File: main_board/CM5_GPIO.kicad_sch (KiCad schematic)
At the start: 32 parts, among them IC4 TS921ID, IC6 TS921ID, J8 AudioJack3

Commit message: Add mounting points to symbols
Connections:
- net GND: now also Module1.MP
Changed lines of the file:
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@@
+	)
+	(junction
+		(at 93.98 160.02)
+		(diameter 0)
+		(color 0 0 0 0)
 	)
 	(junction
@@
 	)
 	(junction
+		(at 59.69 160.02)
+		(diameter 0)
+		(color 0 0 0 0)
+	)
+	(junction
 		(at 59.69 93.98)
 		(diameter 1.016)
@@
 	)
 	(junction
+		(at 123.19 160.02)
+		(diameter 0)
+		(color 0 0 0 0)
+	)
+	(junction
 		(at 123.19 119.38)
 		(diameter 1.016)
@@
 	(wire
 		(pts
+			(xy 59.69 160.02) (xy 93.98 160.02)
+		)
+		(stroke
+			(width 0)
+			(type default)
+		)
+	)
+	(wire
+		(pts
 			(xy 121.92 154.94) (xy 181.61 154.94)
 		)
@@
 			(width 0)
 			(type solid)
+		)
+	)
+	(wire
+		(pts
+			(xy 93.98 160.02) (xy 123.19 160.02)
+		)
+		(stroke
+			(width 0)
+			(type default)
 		)
 	)
@@
 		(pin "200"
 		)
+		(pin "MP"
+		)
 		(instances

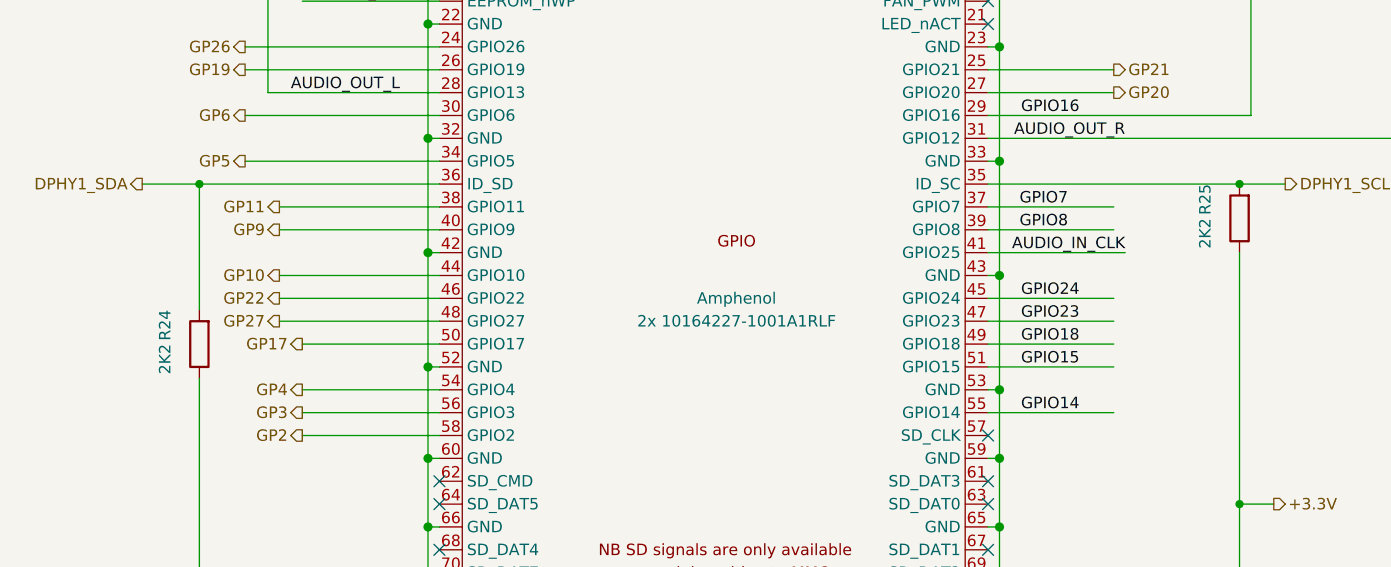
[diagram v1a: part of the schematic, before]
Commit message: Fix bad output voltage
For some reason I got 5V with previous values on prototype. Weird...
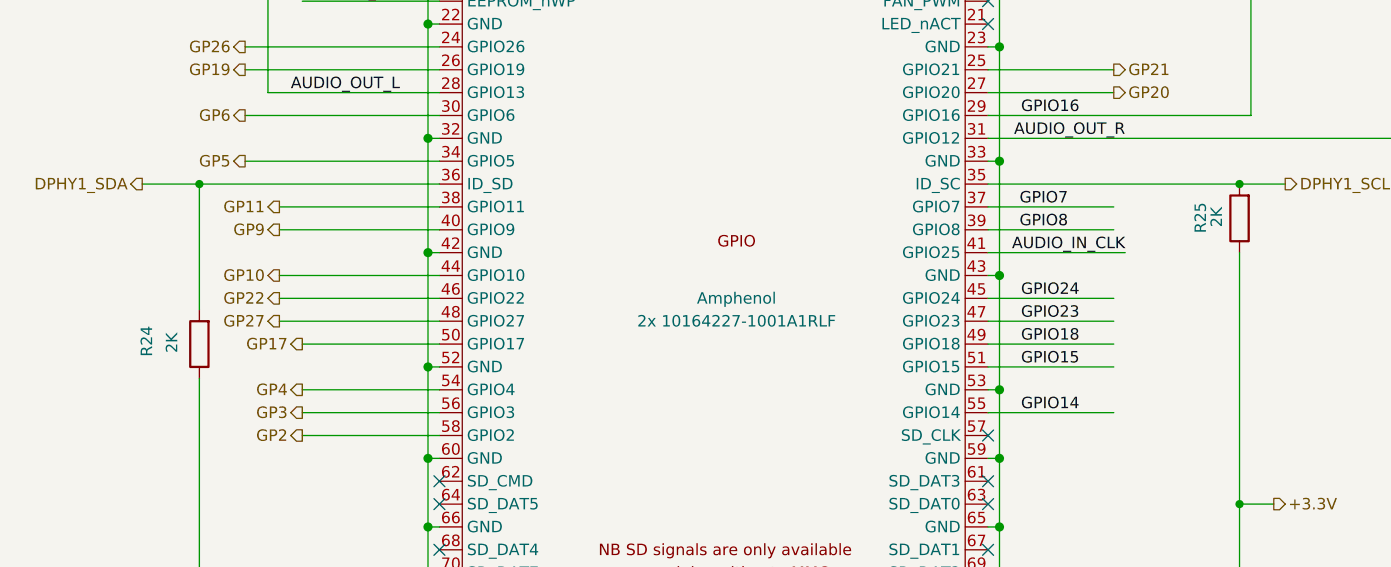
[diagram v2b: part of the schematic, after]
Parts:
- R24, R25: value 2K2 -> 2K
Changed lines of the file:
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@@
 		(dnp no)
 		(property "Reference" "R24"
-			(at 30.48 87.63 90)
+			(at 28.448 89.408 90)
 			(effects
 				(font
@@
 			)
 		)
-		(property "Value" "2K2"
-			(at 30.48 91.44 90)
+		(property "Value" "2K"
+			(at 31.242 90.17 90)
 			(effects
 				(font
@@
 		(dnp no)
 		(property "Reference" "R25"
-			(at 146.05 73.66 90)
+			(at 145.542 75.692 90)
 			(effects
 				(font
@@
 			)
 		)
-		(property "Value" "2K2"
-			(at 146.05 77.47 90)
+		(property "Value" "2K"
+			(at 147.32 76.2 90)
 			(effects
 				(font

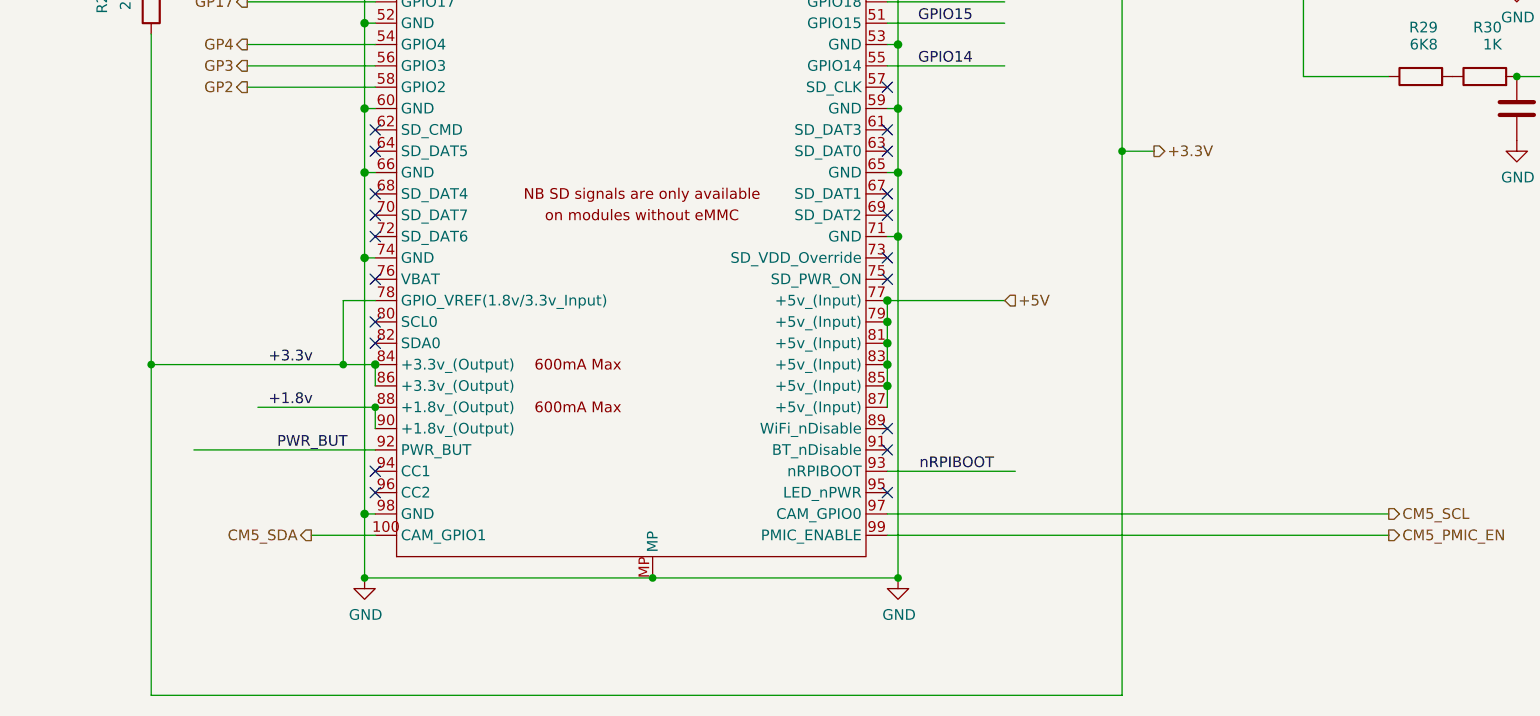
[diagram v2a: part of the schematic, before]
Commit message: Fix critical problems
- Adding USB2 hub on USB3 port did not work correctly
- PM I2C bus was not working when CM5 is shut down
- Missing OTG ID pin
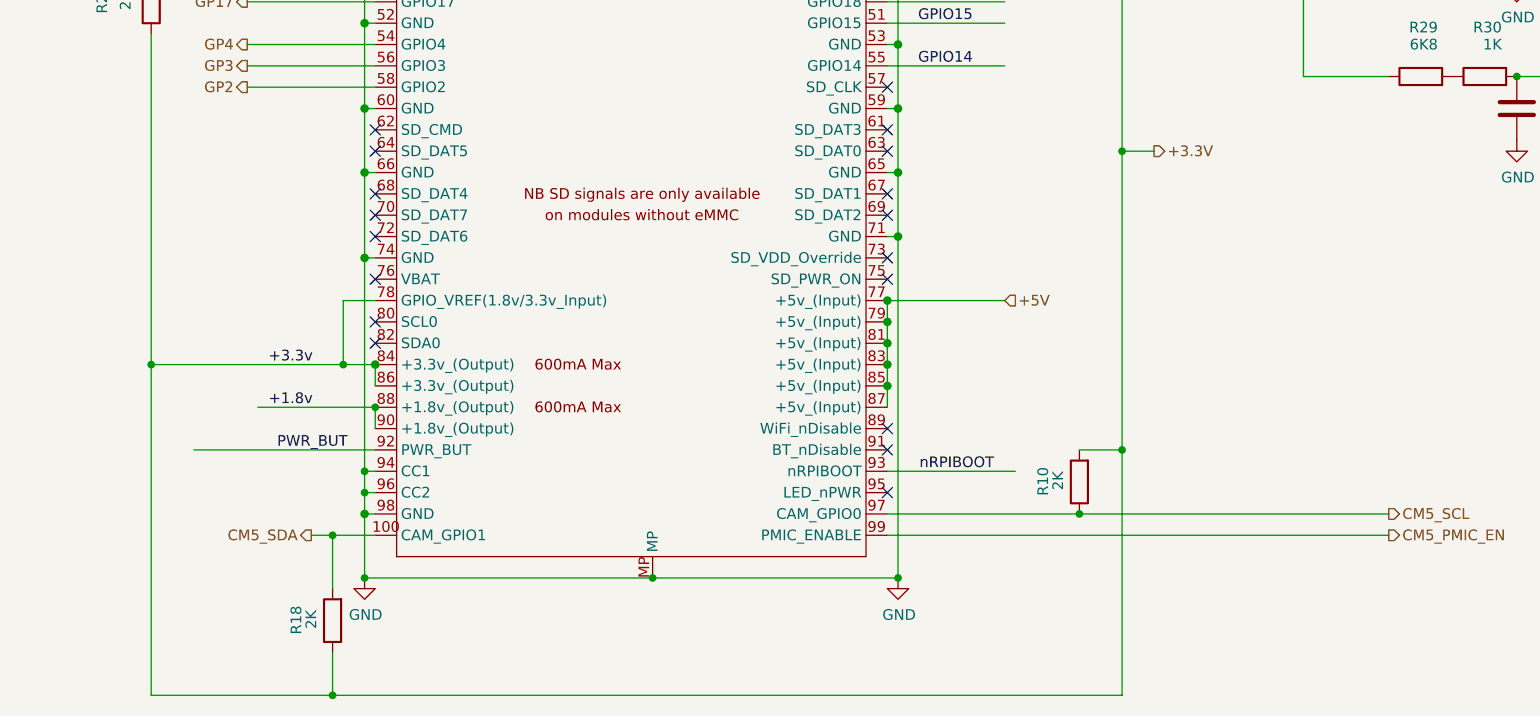
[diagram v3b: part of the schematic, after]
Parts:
- added R10, R18: 2K, Resistor_SMD:R_0805_2012Metric_Pad1.20x1.40mm_HandSolder, symbol Device:R
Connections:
- net +3.3V: now also R10.2, R18.1
- net CM5_SCL: now also R10.1
- net CM5_SDA: now also R18.2
- net GND: now also Module1.94 (CC1), Module1.96 (CC2)
- no-connect marks 34 -> 32

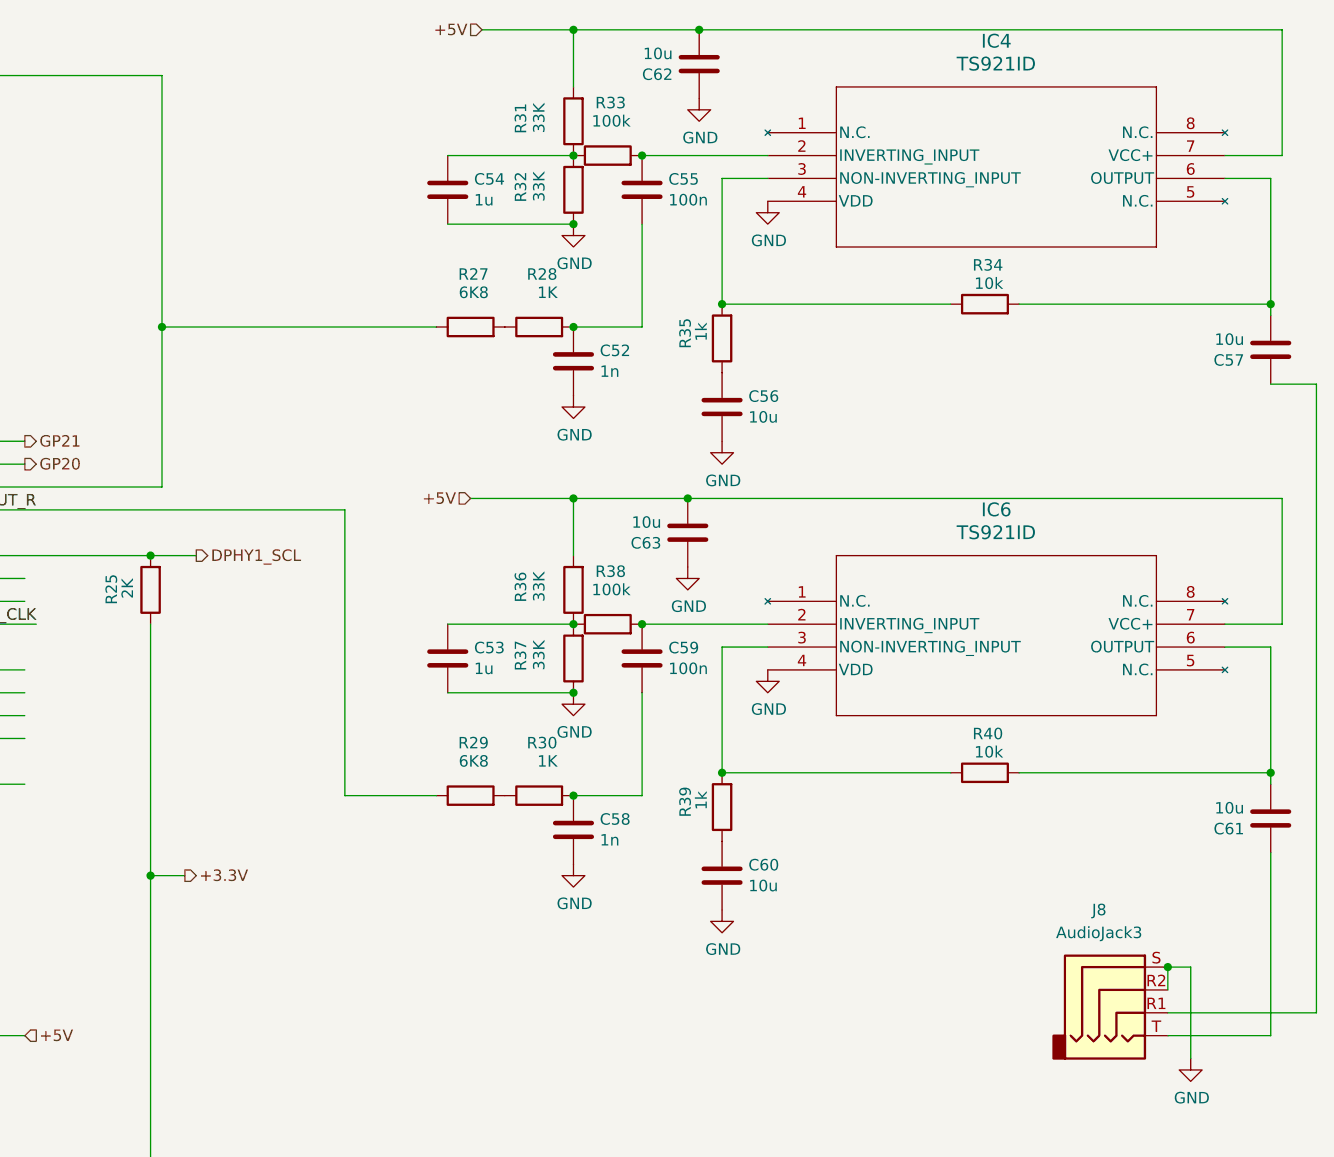
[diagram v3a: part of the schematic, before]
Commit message: Fix CM5 not waking up when enabling boost
When battery is fully charged, CM5 does not turn on.
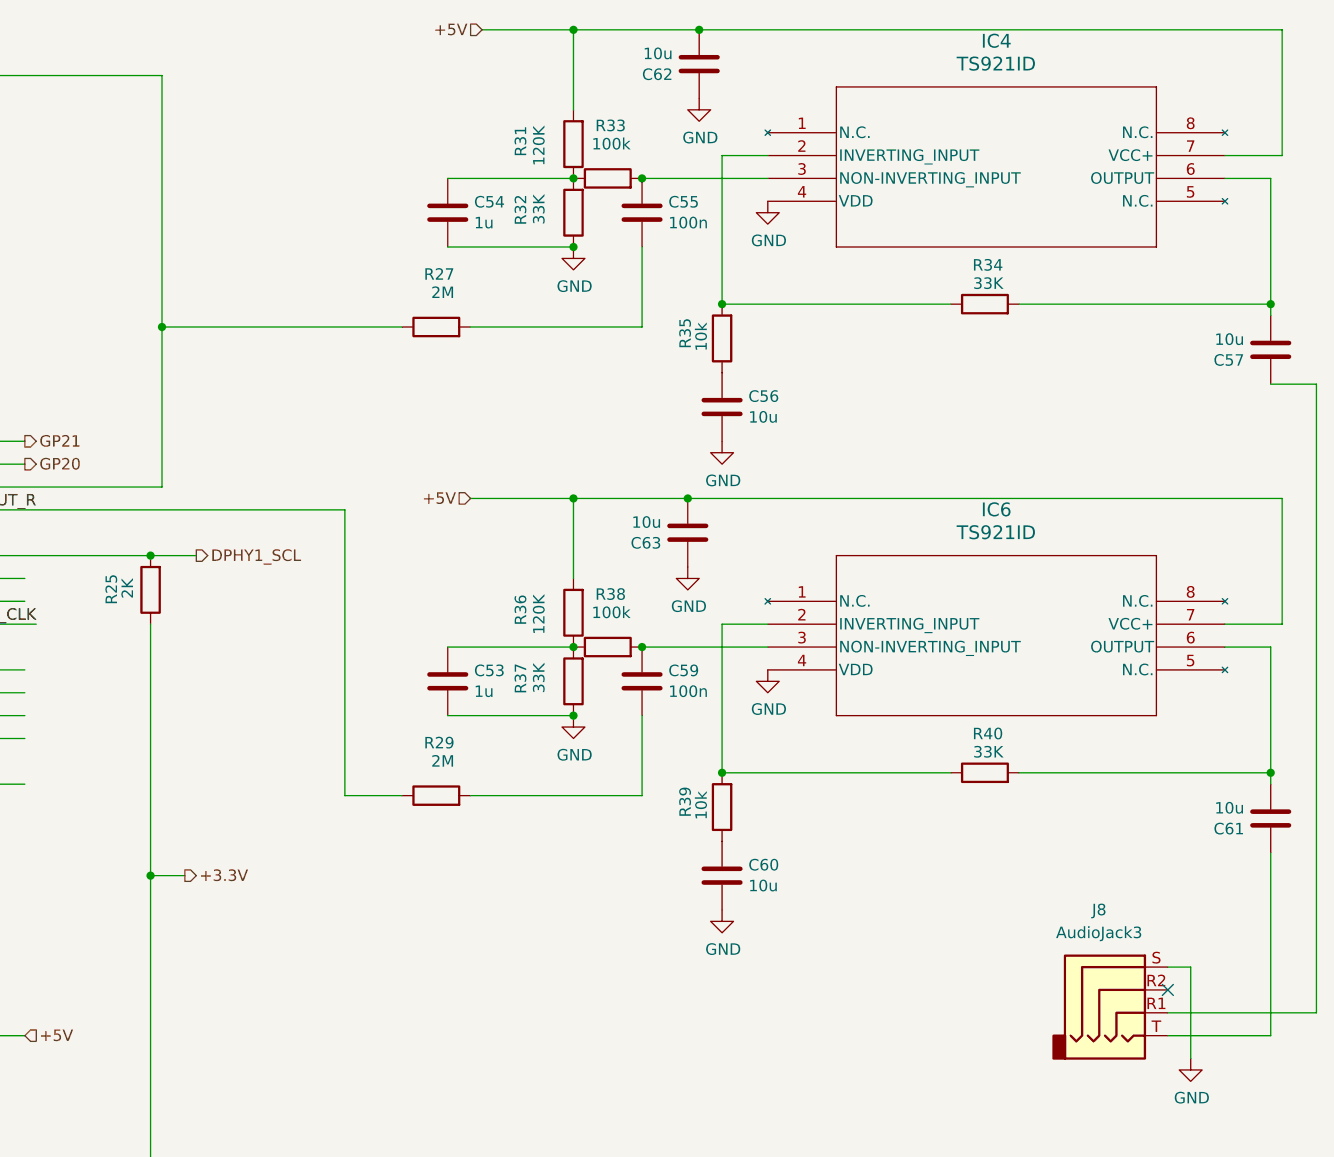
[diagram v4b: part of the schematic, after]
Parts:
- removed C52, C58: 1n, Capacitor_SMD:C_0805_2012Metric_Pad1.18x1.45mm_HandSolder, symbol Device:C
- removed R28, R30: 1K, Resistor_SMD:R_0805_2012Metric_Pad1.20x1.40mm_HandSolder, symbol Device:R
- R27, R29: value 6K8 -> 2M
- R31, R36: value 33K -> 120K
- R34, R40: value 10k -> 33K
- R35, R39: value 1k -> 10k
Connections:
- net GND: no longer J8.R2
- net at R34.1, R35.2: now also IC4.2 (INVERTING_INPUT); no longer IC4.3 (NON-INVERTING_INPUT)
- net at R39.2, R40.1: now also IC6.2 (INVERTING_INPUT); no longer IC6.3 (NON-INVERTING_INPUT)
- net at C55.2: now also R27.2
- net at C55.1, R33.2: now also IC4.3 (NON-INVERTING_INPUT); no longer IC4.2 (INVERTING_INPUT)
- net at C59.1, R38.2: now also IC6.3 (NON-INVERTING_INPUT); no longer IC6.2 (INVERTING_INPUT)
- net at C59.2: now also R29.2
- no-connect marks 32 -> 33
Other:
- moved on the sheet: C53, C54, C55, C59, R27, R29, R31, R32, R33, R36, R37, R38
